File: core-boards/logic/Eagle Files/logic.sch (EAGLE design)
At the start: 67 parts, among them J1 S3B-VH, J2 B2PS-VH(LF)(SN), J3 B2PS-VH(LF)(SN), J4 B2PS-VH(LF)(SN), J5 B2PS-VH(LF)(SN), J6 B2PS-VH(LF)(SN), Q4 STT4P3LLH6, T1 R-78E5.0-1.0, U1 TC4427ACOA713, U2 TXB0106PWRPW16-M, U3 INA198AIDBVR, U4 TLV70233DBVR, U5 MCP2562-I/SN, U6 BMI088, U7 INA198AIDBVR, X1 MINI-USB_SHIELD5P4-32005-400, X10 S6B-EH(LF)(SN), X11 S3B-EH(LF)(SN), X12 B6B-EH-A(LF)(SN), X2 S5B-EH, X3 S5B-EH, X4 B6B-EH-A(LF)(SN), X7 SI-50170, X8 B6B-EH-A(LF)(SN), X9 B6B-EH-A(LF)(SN)

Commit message: logic board revision schemaitcs done
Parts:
- removed C14, C15: 100nF, rcl:C-USC0603
- removed C3: 0.1uF, rcl:C-USC0603
- removed R11: 120, rcl:R-US_R0603
- removed R15: 1k, rcl:R-US_R0603
- removed R16, R17: (no value), rcl:R-US_R0603
- removed U6: BMI088, IGVC-IC:BMI088
- removed X10: S6B-EH(LF)(SN), IGVC-Connector:S6B-EH(LF)(SN)
- added J7: B2PS-VH(LF)(SN), RoboJackets-Connectors:B2PS-VH(LF)(SN)
- R2: value 1M -> 10k
- U5: value MCP2562-I/SN -> MCP2551T-I/SN; device IGVC-Microcontroller:MCP2562-I/SN -> IGVC-Microcontroller:MCP2551T-I/SN
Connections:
- removed net FAN_PWM: X10.X-1, X12.X-3
- removed net N$17: U6.CSB1
- removed net N$3: J1.X-3
- new net NR: A1.P$4, J7.2, R2.1
- net +24V: no longer X10.X-3
- net +3V3: no longer C14.1, C15.1, C3.1, R16.2, R17.2, U5.VI/O, U6.PS, U6.VDD, U6.VDDIO
- net +5V: now also R2.2
- net CANH: now also X12.X-5; no longer R11.1
- net CANL: now also X12.X-6; no longer R11.2
- net CON_CONNECTED: no longer R15.2, X12.X-6
- net DIAG_RX: now also X12.X-4; no longer X12.X-5
- net DIAG_TX: now also X12.X-3; no longer X12.X-4
- net GND: now also J1.X-3, J7.1, U5.RS; no longer C14.2, C15.2, C3.2, R15.1, R2.1, U6.GND, U6.GNDIO, U6.NC, U6.SDO1, U6.SDO2, X10.X-4
- net INT1_ACCEL: no longer U6.INT1
- net INT2_ACCEL: no longer U6.INT2
- net INT3_GYRO: no longer U6.INT3
- net INT4_GYRO: no longer U6.INT4
- net SAFETY_LIGHT: no longer R2.2
- net SCL_3V3: no longer R17.1, U6.SDI
- net SDA_3V3: no longer R16.1, U6.SCK
- net STANDBY: no longer U5.STBY
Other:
- note added: "Make sure this is EM protected"
- note added: "Resistor value between +5V and GND is 560~ therefore the pull up resistor value 10k"
- note added: "Test this"
- note added: "There used to have a BMI088 IMU here. But software has their own odometry source so it's being deprecated"
- note added: "This works without a pull down because mbed handles it"
- note added: "mbed reset Circuit"
- note added: "or Read the PDF manual I wrote"
- note removed: "CSB2 Left Floating in I2C Mode"
- note removed: "Fan Power Connector"
- note removed: "Header Pin S3B-EH-LF-SN; 455-1626-ND S4B-EH-LF-SN;455-1627-ND Connectors: EHR-4;455-1002-ND; EHR-3;455-1001-ND Or reference from digikey page"
- note removed: "If PWM is floating, FAN goes full speed"
- note removed: "Probably too big Resistor"
- note removed: "RPM Signal (X-2) is sensor output from fan and is not used"
- note removed: "Read PWM by low passing it and then read it as analog voltage level"
- note removed: "SDO1 and 2 Grounded for Default I2C Addr"
- moved on the sheet: C4, U5, X11, X12, X3

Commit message: logic board design for internal review :rocket:
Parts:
- removed X1: MINI-USB_SHIELD5P4-32005-400, con-cypressindustries:MINI-USB_SHIELD5P4-32005-400
- removed X11: S3B-EH(LF)(SN), IGVC-Connector:S3B-EH(LF)(SN)
- added J8: B2PS-VH(LF)(SN), RoboJackets-Connectors:B2PS-VH(LF)(SN)
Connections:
- removed net CANH: U5.CANH, X11.TX, X12.X-5
- removed net CANL: U5.CANL, X11.RX, X12.X-6
- removed net CON_CONNECTED: A1.P$21
- removed net D_N: A1.P$32, X1G$1.2
- removed net D_P: A1.P$31, X1G$1.3
- removed net STANDBY: A1.P$22
- new net CAN_N: U5.CANL, X12.X-5
- new net CAN_P: U5.CANH, X12.X-6
- new net STATUS_LED1: A1.P$32, J8.2
- new net STATUS_LED2: A1.P$31, J8.1
- net +5V: no longer X1G$1.1
- net GND: no longer X11.GND, X1G$1.5
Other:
- note added: "NEW"
- note removed: "Pin 4 left empty intentionally"
- note removed: "USBSerial Port"
- moved on the sheet: C4, U5

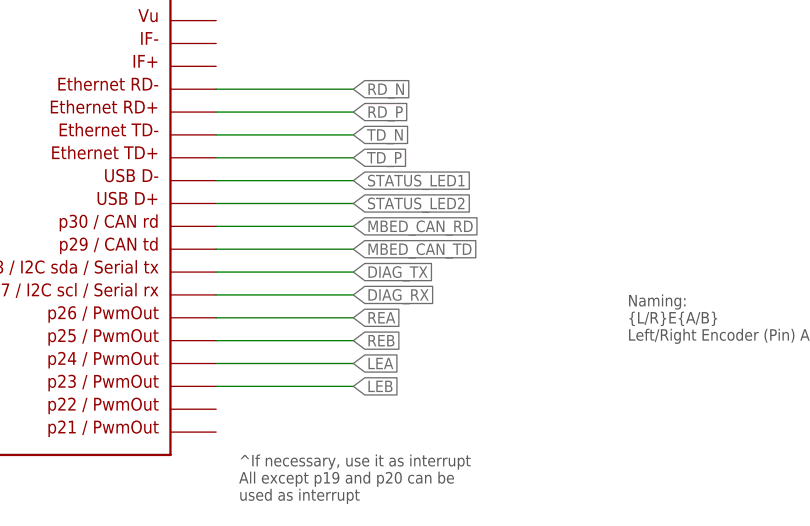
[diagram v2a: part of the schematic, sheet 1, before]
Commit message: Pin inversion fix
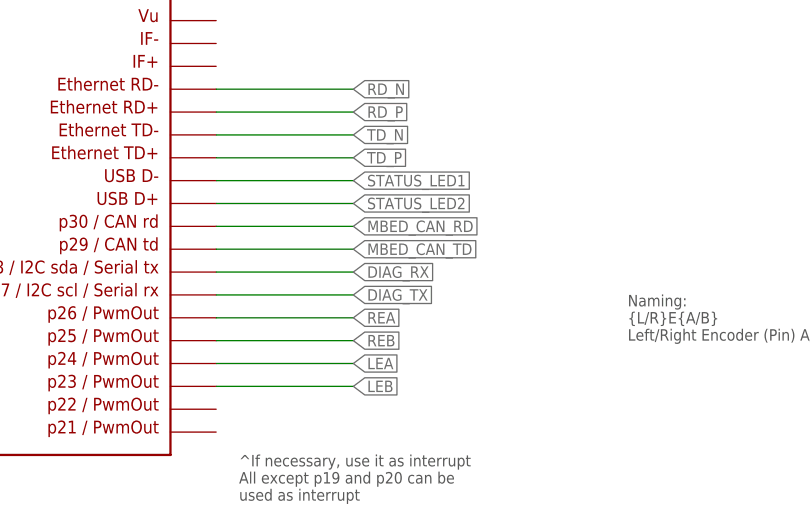
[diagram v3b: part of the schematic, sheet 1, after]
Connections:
- net DIAG_RX: now also A1.P$28; no longer A1.P$27
- net DIAG_TX: now also A1.P$27; no longer A1.P$28
- net MBED_CAN_RD: now also U5.TXD; no longer U5.RXD
- net MBED_CAN_TD: now also U5.RXD; no longer U5.TXD
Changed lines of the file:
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@@
 <net name="DIAG_RX" class="0">
-<segment>
-<pinref part="A1" gate="G$1" pin="P$27"/>
-<wire x1="177.8" y1="104.14" x2="193.04" y2="104.14" width="0.1524" layer="91"/>
-<label x="193.04" y="104.14" size="1.27" layer="95" xref="yes"/>
-</segment>
-</net>
-<net name="DIAG_TX" class="0">
 <segment>
 <wire x1="177.8" y1="106.68" x2="193.04" y2="106.68" width="0.1524" layer="91"/>
@@
 <wire x1="177.8" y1="114.3" x2="193.04" y2="114.3" width="0.1524" layer="91"/>
 <label x="193.04" y="114.3" size="1.27" layer="95" xref="yes"/>
+</segment>
+</net>
+<net name="DIAG_TX" class="0">
+<segment>
+<pinref part="A1" gate="G$1" pin="P$27"/>
+<wire x1="177.8" y1="104.14" x2="193.04" y2="104.14" width="0.1524" layer="91"/>
+<label x="193.04" y="104.14" size="1.27" layer="95" xref="yes"/>
 </segment>
 </net>
@@
 </segment>
 </net>
-<net name="MBED_CAN_TD" class="0">
+<net name="MBED_CAN_RD" class="0">
 <segment>
 <wire x1="60.96" y1="40.64" x2="55.88" y2="40.64" width="0.1524" layer="91"/>
 <label x="55.88" y="40.64" size="1.27" layer="95" rot="R180" xref="yes"/>
 <pinref part="U5" gate="A" pin="TXD"/>
-</segment>
-</net>
-<net name="MBED_CAN_RD" class="0">
-<segment>
-<wire x1="60.96" y1="33.02" x2="58.42" y2="33.02" width="0.1524" layer="91"/>
-<label x="58.42" y="33.02" size="1.27" layer="95" rot="R180" xref="yes"/>
-<pinref part="U5" gate="A" pin="RXD"/>
 </segment>
 </net>
@@
 </segment>
 </net>
+<net name="MBED_CAN_TD" class="0">
+<segment>
+<wire x1="60.96" y1="33.02" x2="58.42" y2="33.02" width="0.1524" layer="91"/>
+<label x="58.42" y="33.02" size="1.27" layer="95" rot="R180" xref="yes"/>
+<pinref part="U5" gate="A" pin="RXD"/>
+</segment>
+</net>

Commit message: design rev
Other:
- note removed: "or Read the PDF manual I wrote"
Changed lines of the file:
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@@
 <text x="16.51" y="125.73" size="1.778" layer="97">This works without a pull down
 because mbed handles it</text>
-<text x="114.3" y="68.58" size="1.778" layer="97">or Read the PDF manual I wrote</text>
 </plain>
 <instances>

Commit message: changes before design rev
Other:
- note added: "External Status LED"
- moved on the sheet: J7, R2
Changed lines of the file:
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@@
 section on this sheet</text>
 <text x="10.16" y="204.47" size="1.778" layer="97">Test this</text>
-<text x="129.54" y="185.42" size="2.54" layer="94">NEW</text>
-<text x="63.5" y="53.34" size="2.54" layer="94">NEW</text>
+<text x="152.4" y="144.78" size="2.54" layer="103" font="vector">External Status LED</text>
 </plain>
 <instances>
@@
 <wire x1="76.2" y1="91.44" x2="76.2" y2="139.7" width="0.1524" layer="103" style="shortdash"/>
 <text x="109.22" y="93.98" size="2.54" layer="103" font="vector">mbed reset Circuit</text>
-<text x="101.6" y="132.08" size="1.778" layer="97">Resistor value between +5V and GND is 560~
+<text x="96.52" y="132.08" size="1.778" layer="97">Resistor value between +5V and GND is 560~
 therefore the pull up resistor value 10k</text>
-<text x="81.28" y="127" size="2.54" layer="94">NEW</text>
 </plain>
 <instances>
@@
 <attribute name="NAME" x="80.645" y="168.91" size="1.778" layer="95"/>
 </instance>
-<instance part="R2" gate="G$1" x="99.06" y="121.92" smashed="yes" rot="R90">
-<attribute name="NAME" x="97.5614" y="118.11" size="1.778" layer="95" rot="R90"/>
-<attribute name="VALUE" x="102.362" y="118.11" size="1.778" layer="96" rot="R90"/>
-</instance>
-<instance part="P+4" gate="1" x="99.06" y="134.62" smashed="yes">
-<attribute name="VALUE" x="96.52" y="129.54" size="1.778" layer="96" rot="R90"/>
-</instance>
-<instance part="GND9" gate="1" x="99.06" y="101.6" smashed="yes">
-<attribute name="VALUE" x="96.52" y="99.06" size="1.778" layer="96"/>
-</instance>
-<instance part="J7" gate="G$1" x="111.76" y="111.76" smashed="yes" rot="R180">
-<attribute name="NAME" x="116.84" y="104.14" size="1.778" layer="95" font="vector" rot="R180" align="top-left"/>
-<attribute name="VALUE" x="104.14" y="116.84" size="1.778" layer="96" font="vector"/>
+<instance part="R2" gate="G$1" x="93.98" y="121.92" smashed="yes" rot="R90">
+<attribute name="NAME" x="92.4814" y="118.11" size="1.778" layer="95" rot="R90"/>
+<attribute name="VALUE" x="97.282" y="118.11" size="1.778" layer="96" rot="R90"/>
+</instance>
+<instance part="P+4" gate="1" x="93.98" y="134.62" smashed="yes">
+<attribute name="VALUE" x="91.44" y="129.54" size="1.778" layer="96" rot="R90"/>
+</instance>
+<instance part="GND9" gate="1" x="93.98" y="101.6" smashed="yes">
+<attribute name="VALUE" x="91.44" y="99.06" size="1.778" layer="96"/>
+</instance>
+<instance part="J7" gate="G$1" x="106.68" y="111.76" smashed="yes" rot="R180">
+<attribute name="NAME" x="111.76" y="104.14" size="1.778" layer="95" font="vector" rot="R180" align="top-left"/>
+<attribute name="VALUE" x="99.06" y="116.84" size="1.778" layer="96" font="vector"/>
 </instance>
 </instances>
@@
 <segment>
 <pinref part="J7" gate="G$1" pin="1"/>
-<wire x1="106.68" y1="109.22" x2="99.06" y2="109.22" width="0.1524" layer="91"/>
+<wire x1="101.6" y1="109.22" x2="93.98" y2="109.22" width="0.1524" layer="91"/>
 <pinref part="GND9" gate="1" pin="GND"/>
-<wire x1="99.06" y1="109.22" x2="99.06" y2="104.14" width="0.1524" layer="91"/>
+<wire x1="93.98" y1="109.22" x2="93.98" y2="104.14" width="0.1524" layer="91"/>
 </segment>
 </net>
@@
 <pinref part="P+4" gate="1" pin="+5V"/>
 <pinref part="R2" gate="G$1" pin="2"/>
-<wire x1="99.06" y1="132.08" x2="99.06" y2="127" width="0.1524" layer="91"/>
+<wire x1="93.98" y1="132.08" x2="93.98" y2="127" width="0.1524" layer="91"/>
 </segment>
 </net>
@@
 <segment>
 <pinref part="J7" gate="G$1" pin="2"/>
-<wire x1="106.68" y1="114.3" x2="99.06" y2="114.3" width="0.1524" layer="91"/>
+<wire x1="101.6" y1="114.3" x2="93.98" y2="114.3" width="0.1524" layer="91"/>
 <pinref part="R2" gate="G$1" pin="1"/>
-<wire x1="99.06" y1="114.3" x2="99.06" y2="116.84" width="0.1524" layer="91"/>
-<wire x1="99.06" y1="114.3" x2="93.98" y2="114.3" width="0.1524" layer="91"/>
-<junction x="99.06" y="114.3"/>
-<label x="93.98" y="114.3" size="1.27" layer="95" rot="R180" xref="yes"/>
-</segment>
-</net>
+<wire x1="93.98" y1="114.3" x2="93.98" y2="116.84" width="0.1524" layer="91"/>
+<wire x1="93.98" y1="114.3" x2="88.9" y2="114.3" width="0.1524" layer="91"/>
+<junction x="93.98" y="114.3"/>
+<label x="88.9" y="114.3" size="1.27" layer="95" rot="R180" xref="yes"/>
+</segment>
+</net>

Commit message: Schematics rev Done
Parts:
- added C14, C15: 0.1uF, rcl:C-USC0603
- added C3: 1uF, rcl:C-USC0805
- added U6: D5V0L1B2WS-7, IGVC-Discrete:D5V0L1B2WS-7
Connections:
- new net N$3: C3.1, J7.1
- new net V+: J4.2, U6.EPAD_2
- net +12V: no longer J4.2
- net +3V3: no longer R5.2, U2.VCCA
- net GND: now also C14.2, C15.2, C3.2, R5.2, U1.IN_A, U2.VCCA, U6.EPAD; no longer J7.1, X7.C, X7.C1
- net SCL_5V: now also C14.1
- net SDA_5V: now also C15.1
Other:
- note added: "R9 and R10 are special type shunt resistor, value 50mOhm"
- note added: "Switch Config: HLHLLH"
- note added: "TVS Diode for Clamping Voltage"
- moved on the sheet: D1, J1, J4, J8, R1, R5, U2

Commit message: Routing rev finished
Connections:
- removed net V+: J4.2, U6.EPAD_2
- net +12V: now also J4.2, U6.EPAD_2
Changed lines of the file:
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@@
 <pinref part="SUPPLY6" gate="1" pin="V+"/>
+</segment>
+<segment>
+<pinref part="J4" gate="G$1" pin="2"/>
+<wire x1="93.345" y1="179.07" x2="81.28" y2="179.07" width="0.1524" layer="91"/>
+<wire x1="81.28" y1="185.42" x2="81.28" y2="179.07" width="0.1524" layer="91"/>
+<pinref part="SUPPLY5" gate="1" pin="V+"/>
+<wire x1="66.04" y1="187.96" x2="66.04" y2="185.42" width="0.1524" layer="91"/>
+<wire x1="66.04" y1="185.42" x2="81.28" y2="185.42" width="0.1524" layer="91"/>
+<pinref part="U6" gate="A" pin="EPAD_2"/>
+<wire x1="48.26" y1="175.26" x2="50.8" y2="175.26" width="0.1524" layer="91"/>
+<wire x1="48.26" y1="185.42" x2="48.26" y2="175.26" width="0.1524" layer="91"/>
+<wire x1="66.04" y1="185.42" x2="48.26" y2="185.42" width="0.1524" layer="91"/>
+<junction x="66.04" y="185.42"/>
 </segment>
 </net>
@@
 </segment>
 </net>
-<net name="V+" class="0">
-<segment>
-<pinref part="J4" gate="G$1" pin="2"/>
-<wire x1="93.345" y1="179.07" x2="81.28" y2="179.07" width="0.1524" layer="91"/>
-<wire x1="81.28" y1="185.42" x2="81.28" y2="179.07" width="0.1524" layer="91"/>
-<pinref part="SUPPLY5" gate="1" pin="V+"/>
-<wire x1="66.04" y1="187.96" x2="66.04" y2="185.42" width="0.1524" layer="91"/>
-<wire x1="66.04" y1="185.42" x2="81.28" y2="185.42" width="0.1524" layer="91"/>
-<pinref part="U6" gate="A" pin="EPAD_2"/>
-<wire x1="48.26" y1="175.26" x2="50.8" y2="175.26" width="0.1524" layer="91"/>
-<wire x1="48.26" y1="185.42" x2="48.26" y2="175.26" width="0.1524" layer="91"/>
-<wire x1="66.04" y1="185.42" x2="48.26" y2="185.42" width="0.1524" layer="91"/>
-<junction x="66.04" y="185.42"/>
-</segment>
-</net>

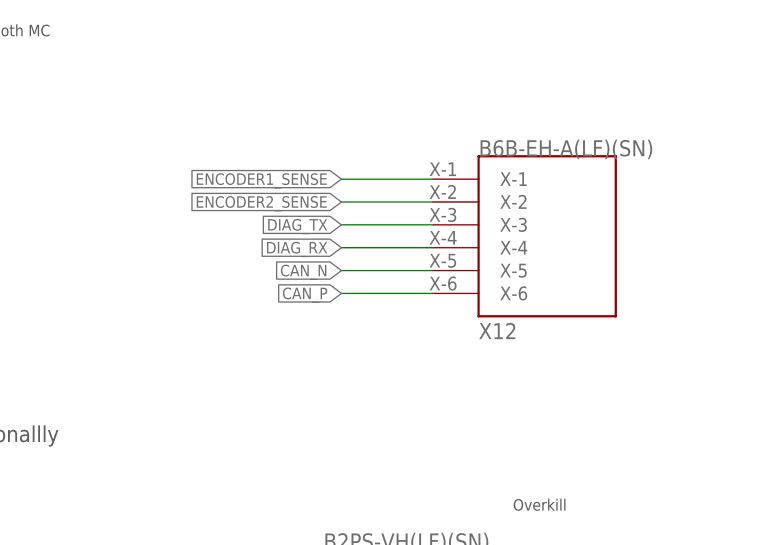
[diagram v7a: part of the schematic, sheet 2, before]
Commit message: Fixing connector type
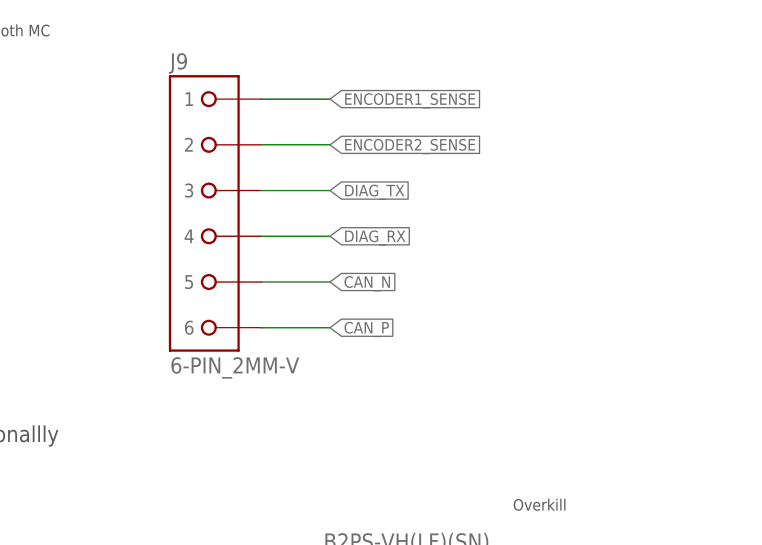
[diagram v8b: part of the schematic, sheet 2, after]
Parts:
- removed X12: B6B-EH-A(LF)(SN), IGVC-Connector:B6B-EH-A(LF)(SN)
- added J9: 6-PIN_2MM-V, RoboJackets-Connectors:6-PIN_2MM-V
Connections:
- net CAN_N: now also J9.5; no longer X12.X-5
- net CAN_P: now also J9.6; no longer X12.X-6
- net DIAG_RX: now also J9.4; no longer X12.X-4
- net DIAG_TX: now also J9.3; no longer X12.X-3
- net ENCODER1_SENSE: now also J9.1; no longer X12.X-1
- net ENCODER2_SENSE: now also J9.2; no longer X12.X-2
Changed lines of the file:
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@@
 <part name="P+10" library="supply1" library_urn="urn:adsk.eagle:library:371" deviceset="+5V" device=""/>
 <part name="SUPPLY6" library="supply2" library_urn="urn:adsk.eagle:library:372" deviceset="V+" device="" value="+12V"/>
-<part name="X12" library="IGVC-Connector" deviceset="B6B-EH-A(LF)(SN)" device=""/>
 <part name="+3V3" library="supply1" library_urn="urn:adsk.eagle:library:371" deviceset="+3V3" device=""/>
 <part name="P+12" library="supply1" library_urn="urn:adsk.eagle:library:371" deviceset="+5V" device=""/>
@@
 <part name="GND10" library="supply1" library_urn="urn:adsk.eagle:library:371" deviceset="GND" device=""/>
 <part name="U6" library="IGVC-Discrete" deviceset="D5V0L1B2WS-7" device=""/>
+<part name="J9" library="RoboJackets-Connectors" deviceset="6-PIN_2MM-*" device="V"/>
 </parts>
 <sheets>
@@
 <attribute name="VALUE" x="147.32" y="127" size="1.778" layer="96"/>
 </instance>
-<instance part="X12" gate="G$1" x="163.83" y="171.45" smashed="yes">
-<attribute name="VALUE" x="163.83" y="189.23" size="1.778" layer="96"/>
-<attribute name="NAME" x="163.83" y="168.91" size="1.778" layer="95"/>
-</instance>
 <instance part="U7" gate="A" x="40.64" y="104.14" smashed="yes">
 <attribute name="NAME" x="43.18" y="106.68" size="2.0828" layer="95" ratio="6" rot="SR0"/>
@@
 <attribute name="VALUE" x="78.74" y="134.62" size="1.778" layer="96" rot="R180"/>
 <attribute name="NAME" x="78.74" y="152.4" size="1.778" layer="95" rot="R180"/>
+</instance>
+<instance part="J9" gate="G$1" x="134.62" y="182.88" smashed="yes">
+<attribute name="NAME" x="129.54" y="200.66" size="1.778" layer="95" font="vector" align="top-left"/>
+<attribute name="VALUE" x="129.54" y="165.1" size="1.778" layer="96" font="vector"/>
 </instance>
 </instances>
@@
 <net name="ENCODER1_SENSE" class="0">
 <segment>
-<wire x1="158.75" y1="186.69" x2="148.59" y2="186.69" width="0.1524" layer="91"/>
-<label x="148.59" y="186.69" size="1.27" layer="95" rot="R180" xref="yes"/>
-<pinref part="X12" gate="G$1" pin="X-1"/>
-</segment>
-<segment>
 <pinref part="U7" gate="A" pin="OUT"/>
 <wire x1="35.56" y1="99.06" x2="30.48" y2="99.06" width="0.1524" layer="91"/>
 <label x="30.48" y="99.06" size="1.27" layer="95" rot="R180" xref="yes"/>
 </segment>
+<segment>
+<pinref part="J9" gate="G$1" pin="1"/>
+<wire x1="139.7" y1="195.58" x2="147.32" y2="195.58" width="0.1524" layer="91"/>
+<label x="147.32" y="195.58" size="1.27" layer="95" xref="yes"/>
+</segment>
 </net>
 <net name="ENCODER2_SENSE" class="0">
-<segment>
-<wire x1="158.75" y1="184.15" x2="148.59" y2="184.15" width="0.1524" layer="91"/>
-<label x="148.59" y="184.15" size="1.27" layer="95" rot="R180" xref="yes"/>
-<pinref part="X12" gate="G$1" pin="X-2"/>
-</segment>
 <segment>
 <pinref part="U3" gate="A" pin="OUT"/>
 <wire x1="35.56" y1="71.12" x2="30.48" y2="71.12" width="0.1524" layer="91"/>
 <label x="30.48" y="71.12" size="1.27" layer="95" rot="R180" xref="yes"/>
+</segment>
+<segment>
+<pinref part="J9" gate="G$1" pin="2"/>
+<wire x1="139.7" y1="190.5" x2="147.32" y2="190.5" width="0.1524" layer="91"/>
+<label x="147.32" y="190.5" size="1.27" layer="95" xref="yes"/>
 </segment>
 </net>
@@
 <net name="DIAG_TX" class="0">
 <segment>
-<pinref part="X12" gate="G$1" pin="X-3"/>
-<wire x1="158.75" y1="181.61" x2="148.59" y2="181.61" width="0.1524" layer="91"/>
-<label x="148.59" y="181.61" size="1.27" layer="95" rot="R180" xref="yes"/>
+<pinref part="J9" gate="G$1" pin="3"/>
+<wire x1="139.7" y1="185.42" x2="147.32" y2="185.42" width="0.1524" layer="91"/>
+<label x="147.32" y="185.42" size="1.27" layer="95" xref="yes"/>
 </segment>
 </net>
 <net name="DIAG_RX" class="0">
 <segment>
-<pinref part="X12" gate="G$1" pin="X-4"/>
-<wire x1="158.75" y1="179.07" x2="148.59" y2="179.07" width="0.1524" layer="91"/>
-<label x="148.59" y="179.07" size="1.27" layer="95" rot="R180" xref="yes"/>
+<pinref part="J9" gate="G$1" pin="4"/>
+<wire x1="139.7" y1="180.34" x2="147.32" y2="180.34" width="0.1524" layer="91"/>
+<label x="147.32" y="180.34" size="1.27" layer="95" xref="yes"/>
 </segment>
 </net>
 <net name="CAN_N" class="0">
 <segment>
-<pinref part="X12" gate="G$1" pin="X-5"/>
-<wire x1="158.75" y1="176.53" x2="148.59" y2="176.53" width="0.1524" layer="91"/>
-<label x="148.59" y="176.53" size="1.27" layer="95" rot="R180" xref="yes"/>
+<pinref part="J9" gate="G$1" pin="5"/>
+<wire x1="139.7" y1="175.26" x2="147.32" y2="175.26" width="0.1524" layer="91"/>
+<label x="147.32" y="175.26" size="1.27" layer="95" xref="yes"/>
 </segment>
 </net>
 <net name="CAN_P" class="0">
 <segment>
-<pinref part="X12" gate="G$1" pin="X-6"/>
-<wire x1="158.75" y1="173.99" x2="148.59" y2="173.99" width="0.1524" layer="91"/>
-<label x="148.59" y="173.99" size="1.27" layer="95" rot="R180" xref="yes"/>
-</segment>
-</net>
+<pinref part="J9" gate="G$1" pin="6"/>
+<wire x1="139.7" y1="170.18" x2="147.32" y2="170.18" width="0.1524" layer="91"/>
+<label x="147.32" y="170.18" size="1.27" layer="95" xref="yes"/>
+</segment>
+</net>
